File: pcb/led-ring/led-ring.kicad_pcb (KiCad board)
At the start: 2 copper layers, 30 x 30 mm, 31 parts, among them P1 CONN_01X12

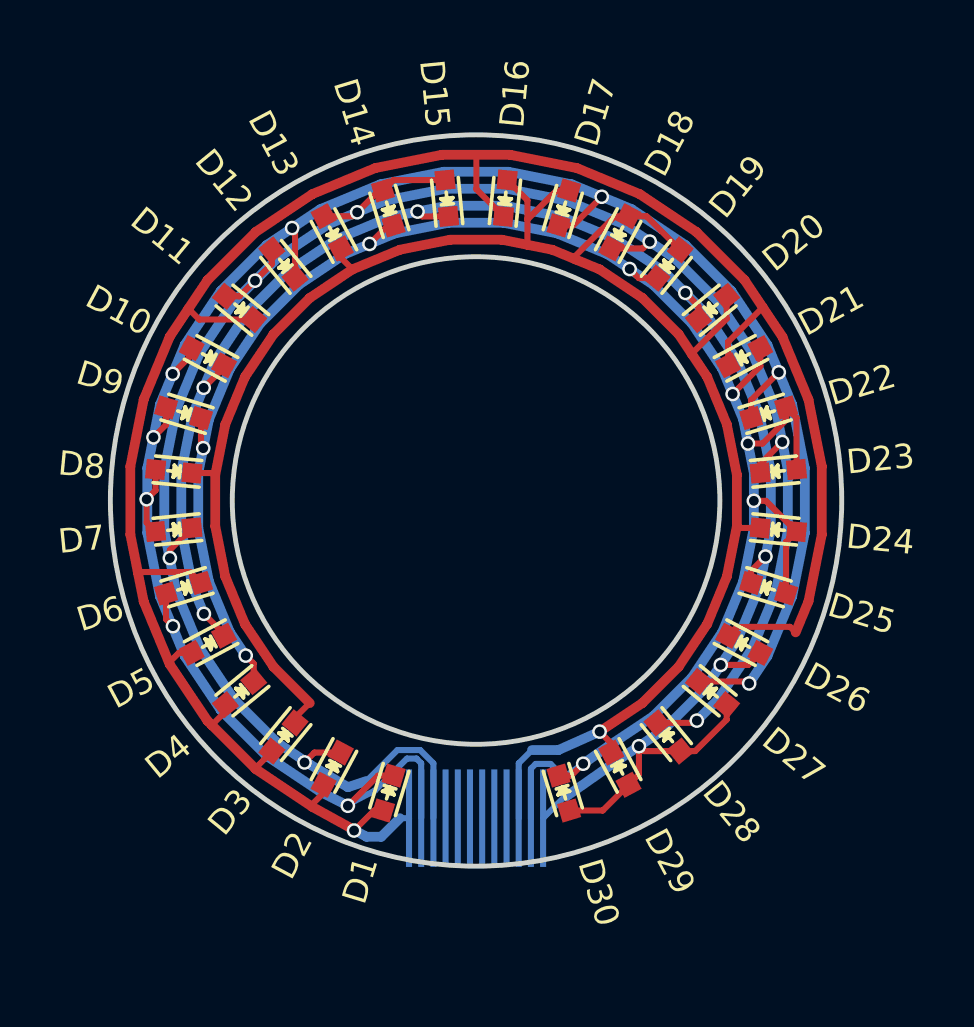
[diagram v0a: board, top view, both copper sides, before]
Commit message: o Add IR receiver. o Shape ring in a way so that receiver fits.
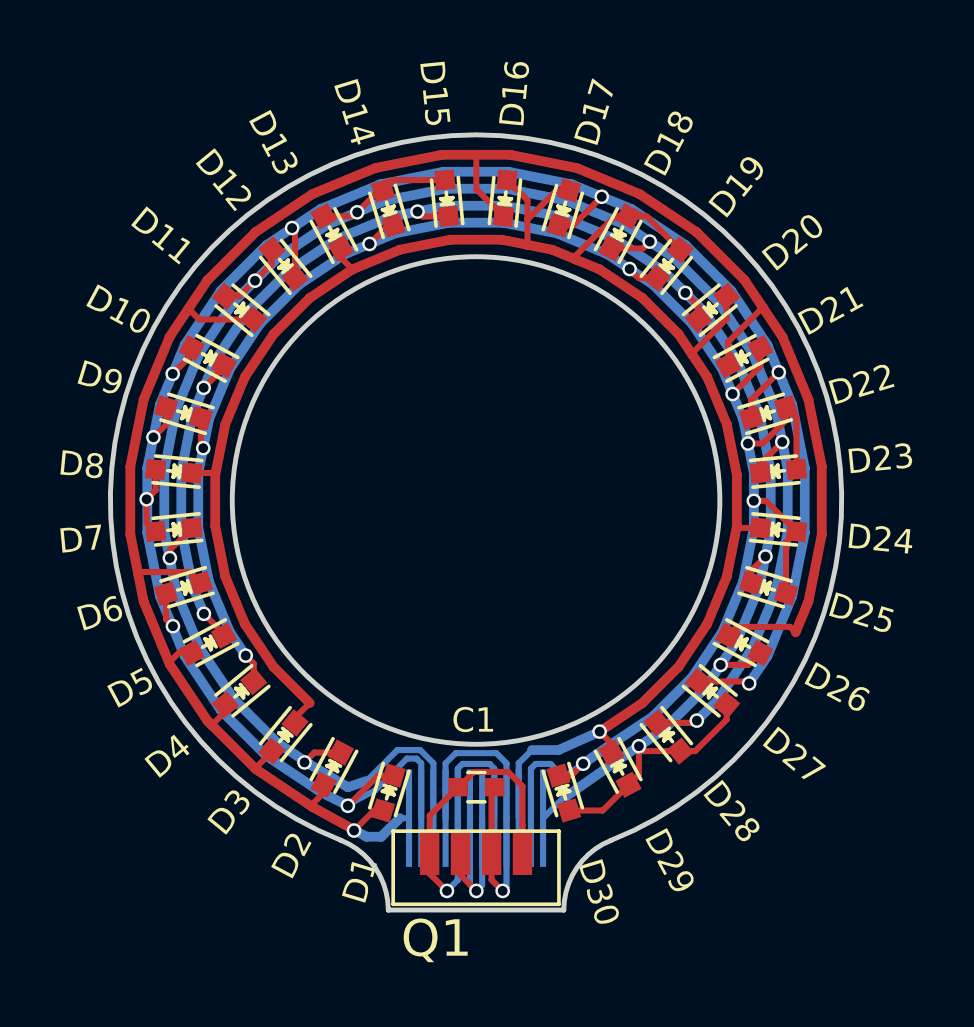
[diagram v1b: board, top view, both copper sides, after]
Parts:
- added C1: 100n, Capacitors_SMD:C_0603, F.Cu at (100.0, 111.8)
- added Q1: TSOP75338, knopf:TSOP75xx, F.Cu at (100.0, 115.1)
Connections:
- P1 pad 4: (no net) -> /VCC
- P1 pad 5: (no net) -> /GND
- P1 pad 6: (no net) -> /IR-signal
- P1 pad 7: (no net) -> /IR-signal
- P1 pad 8: (no net) -> /GND
- P1 pad 9: (no net) -> /VCC
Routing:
- net /GND: track 0.00 -> 19.8 mm, vias 0 -> 1
- net /VCC: track 0.00 -> 14.9 mm, vias 0 -> 1
- net /IR-signal: track 0.00 -> 8.00 mm, vias 0 -> 1
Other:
- board size 30 x 30 mm -> 30 x 31.8 mm
- board text added: "%%gitversion%%"
- board text added: "github hzeller/DerKnopf"

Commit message: led-ring: Update to Kicad 7
 * Use new schematic symbols and footprints
 * adjust board configuration for good solder stop expansion
 * Update Python script to work with current kicad.
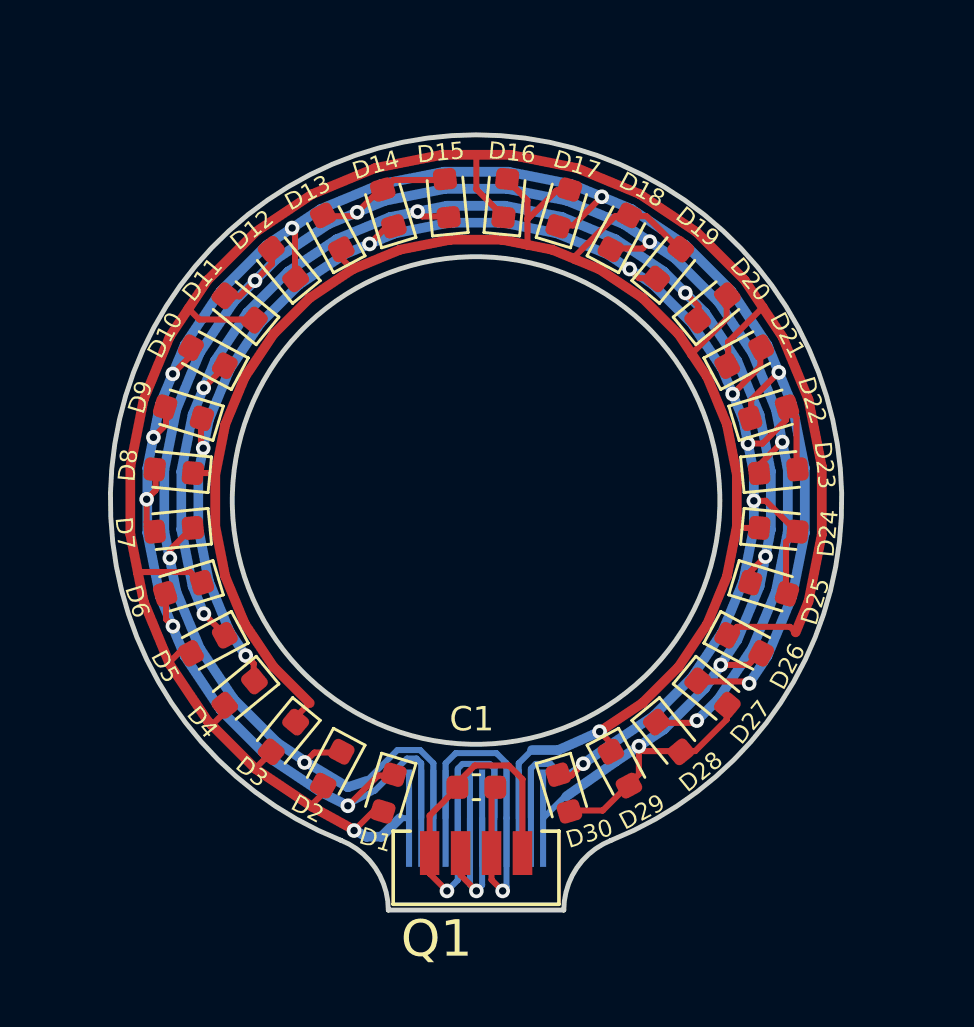
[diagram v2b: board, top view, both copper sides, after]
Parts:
- C1: footprint Capacitors_SMD:C_0603 -> Capacitor_SMD:C_0603_1608Metric
- D1, D10, D11, D12, D13, D14, D15, D16, D17, D18, D19, D2, D20, D21, D22, D23, D24, D25, D26, D27, D28, D29, D3, D30, D4, D5, D6, D7, D8, D9: footprint LEDs:LED_0603 -> LED_SMD:LED_0603_1608Metric
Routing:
- net /GND: track 19.8 -> 20.4 mm
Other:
- net class Default removed
- rule pad_to_mask_clearance: 0.2 -> 0.08
